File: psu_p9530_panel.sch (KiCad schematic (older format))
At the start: 56 parts, among them IC306 LTC1658, IC308 CD4052B, IC310 TLC272, IC312 TLC272, U401 74HCT164

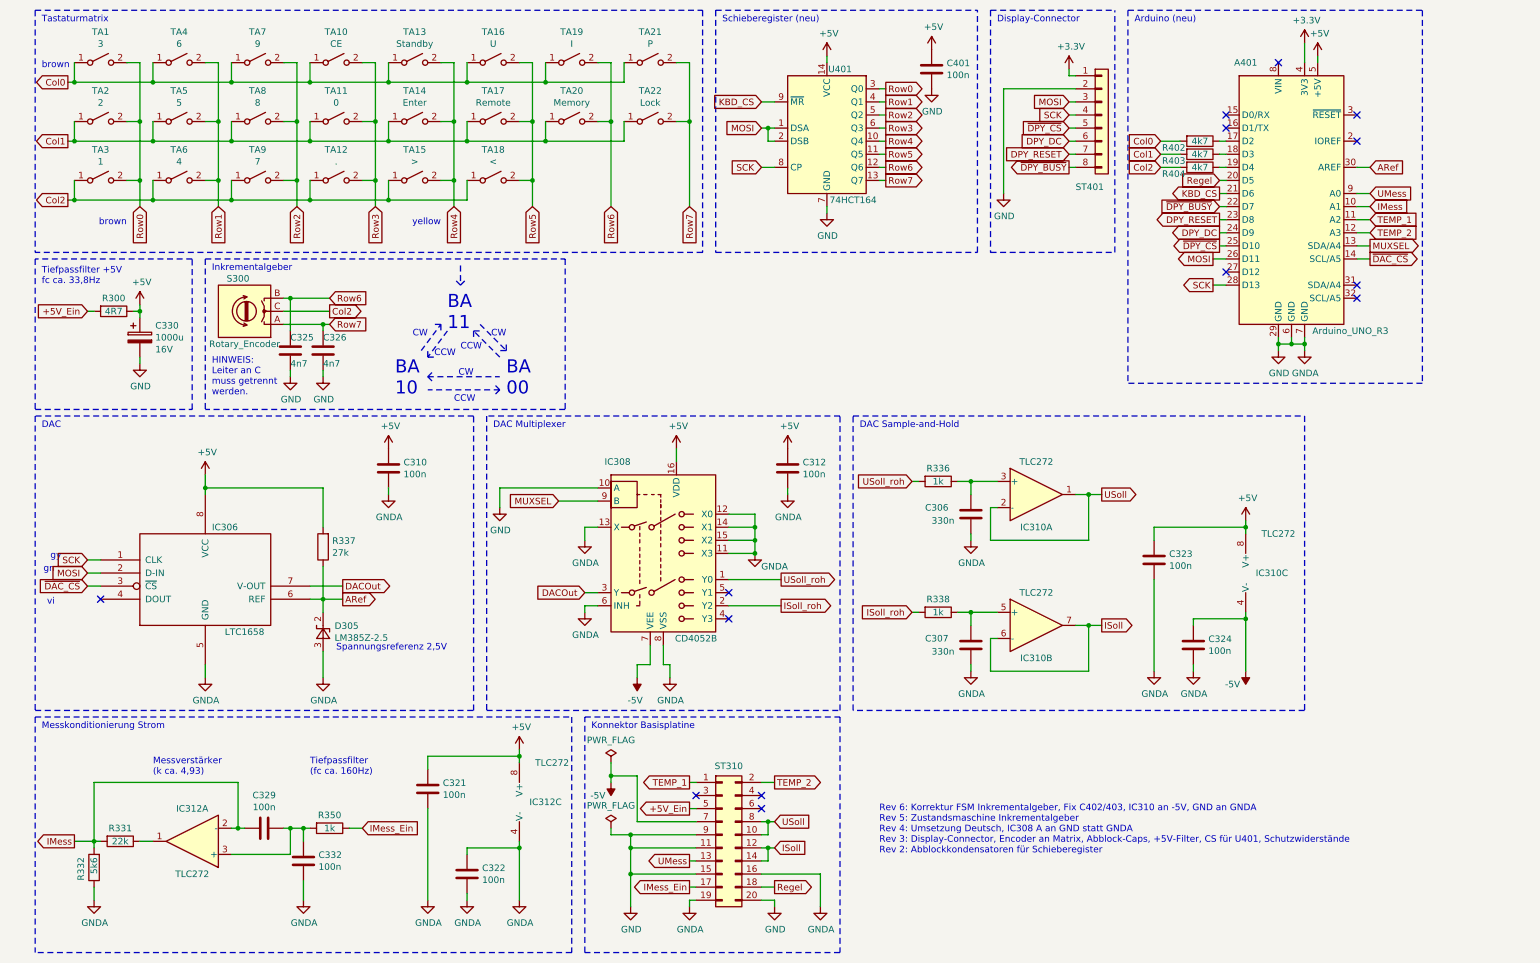
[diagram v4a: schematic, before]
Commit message: Add note about using 54LS164 for the shift register - after half a day of investigations
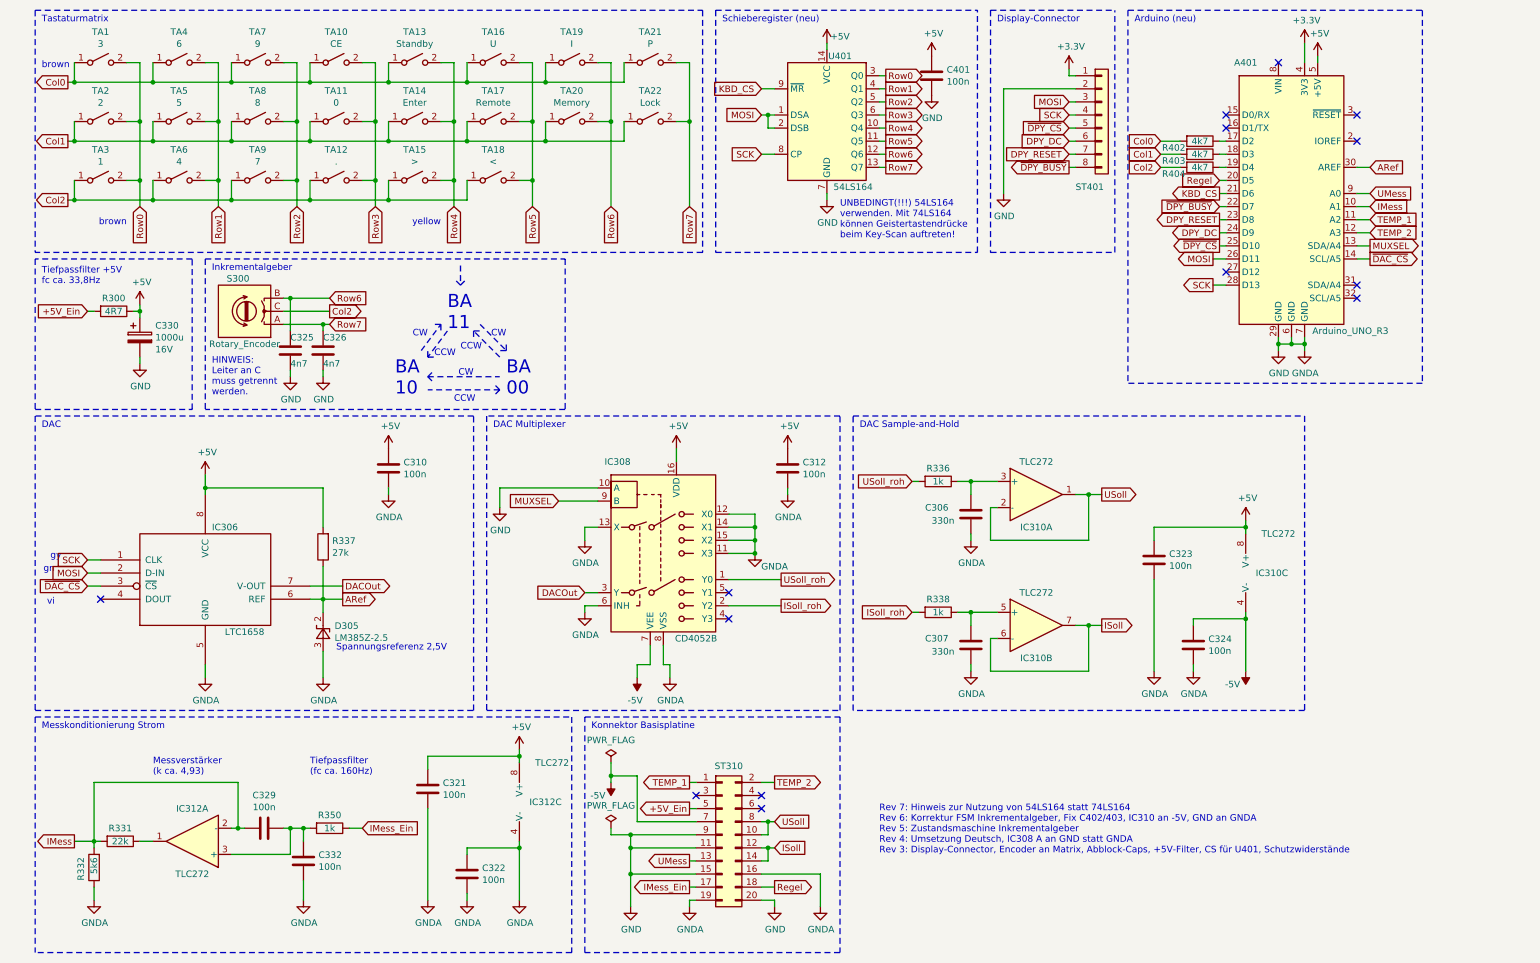
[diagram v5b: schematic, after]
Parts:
- U401: value 74HCT164 -> 54LS164
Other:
- note added: "Rev 7: Hinweis zur Nutzung von 54LS164 statt 74LS164\nRev 6: Korrektur FSM Inkrementalgeber, Fix C402/403, IC310 an -5V, GND an GNDA\nRev 5: Zustandsmaschine Inkrementalgeber\nRev 4: Umsetzung Deutsch, IC308 A an GND statt GNDA\nRev 3: Display-Connector, Encoder an Matrix, Abblock-Caps, +5V-Filter, CS für U401, Schutzwiderstände"
- note added: "UNBEDINGT(!!!) 54LS164\nverwenden. Mit 74LS164\nkönnen Geistertastendrücke\nbeim Key-Scan auftreten!"
- note removed: "Rev 6: Korrektur FSM Inkrementalgeber, Fix C402/403, IC310 an -5V, GND an GNDA\nRev 5: Zustandsmaschine Inkrementalgeber\nRev 4: Umsetzung Deutsch, IC308 A an GND statt GNDA\nRev 3: Display-Connector, Encoder an Matrix, Abblock-Caps, +5V-Filter, CS für U401, Schutzwiderstände\nRev 2: Abblockkondensatoren für Schieberegister"
- moved on the sheet: C401, U401
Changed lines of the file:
@@
 Title "ELV PS9530 Ersatz Bedienteil"
 Date "2022-08-20"
-Rev "6"
+Rev "7"
 Comp "Ralf Gerlich"
 Comment1 ""
@@
 L power:+5V #PWR0126
 U 1 1 6362FD60
-P 6600 900
-F 0 "#PWR0126" H 6600 750 50  0001 C CNN
-F 1 "+5V" H 6615 1073 50  0000 C CNN
-F 2 "" H 6600 900 50  0001 C CNN
-F 3 "" H 6600 900 50  0001 C CNN
-	1    6600 900
-	1    0    0    -1
-$EndComp
-Text GLabel 6100 1750 0    50   Input ~ 0
+P 6600 800
+F 0 "#PWR0126" H 6600 650 50  0001 C CNN
+F 1 "+5V" H 6700 850 50  0000 C CNN
+F 2 "" H 6600 800 50  0001 C CNN
+F 3 "" H 6600 800 50  0001 C CNN
+	1    6600 800
+	1    0    0    -1
+$EndComp
+Text GLabel 6100 1650 0    50   Input ~ 0
 SCK
-Text GLabel 6100 1450 0    50   Input ~ 0
+Text GLabel 6100 1350 0    50   Input ~ 0
 MOSI
+Text GLabel 7050 1050 2    50   Output ~ 0
+Row0
+Wire Wire Line
+	7050 1050 7000 1050
 Text GLabel 7050 1150 2    50   Output ~ 0
-Row0
+Row1
+Text GLabel 7050 1250 2    50   Output ~ 0
+Row2
+Text GLabel 7050 1350 2    50   Output ~ 0
+Row3
+Text GLabel 7050 1450 2    50   Output ~ 0
+Row4
+Text GLabel 7050 1550 2    50   Output ~ 0
+Row5
+Text GLabel 7050 1650 2    50   Output ~ 0
+Row6
+Text GLabel 7050 1750 2    50   Output ~ 0
+Row7
+Wire Wire Line
+	7050 1750 7000 1750
+Wire Wire Line
+	7050 1650 7000 1650
+Wire Wire Line
+	7050 1550 7000 1550
+Wire Wire Line
+	7050 1450 7000 1450
+Wire Wire Line
+	7050 1350 7000 1350
+Wire Wire Line
+	7050 1250 7000 1250
 Wire Wire Line
 	7050 1150 7000 1150
-Text GLabel 7050 1250 2    50   Output ~ 0
-Row1
-Text GLabel 7050 1350 2    50   Output ~ 0
-Row2
-Text GLabel 7050 1450 2    50   Output ~ 0
-Row3
-Text GLabel 7050 1550 2    50   Output ~ 0
-Row4
-Text GLabel 7050 1650 2    50   Output ~ 0
-Row5
-Text GLabel 7050 1750 2    50   Output ~ 0
-Row6
-Text GLabel 7050 1850 2    50   Output ~ 0
-Row7
-Wire Wire Line
-	7050 1850 7000 1850
-Wire Wire Line
-	7050 1750 7000 1750
-Wire Wire Line
-	7050 1650 7000 1650
-Wire Wire Line
-	7050 1550 7000 1550
-Wire Wire Line
-	7050 1450 7000 1450
-Wire Wire Line
-	7050 1350 7000 1350
-Wire Wire Line
-	7050 1250 7000 1250
 Text GLabel 10750 2350 2    50   Output ~ 0
 MUXSEL
@@
 L 74xx:74HCT164 U401
 U 1 1 637BAC19
-P 6600 1450
-F 0 "U401" H 6700 1900 50  0000 C CNN
-F 1 "74HCT164" H 6800 900 50  0000 C CNN
-F 2 "" H 7500 1150 50  0001 C CNN
-F 3 "https://assets.nexperia.com/documents/data-sheet/74HC_HCT164.pdf" H 7500 1150 50  0001 C CNN
-	1    6600 1450
-	1    0    0    -1
-$EndComp
-Wire Wire Line
-	6100 1450 6150 1450
-Wire Wire Line
-	6150 1450 6150 1550
-Wire Wire Line
-	6150 1550 6200 1550
-Connection ~ 6150 1450
+P 6600 1350
+F 0 "U401" H 6700 1800 50  0000 C CNN
+F 1 "54LS164" H 6800 800 50  0000 C CNN
+F 2 "" H 7500 1050 50  0001 C CNN
+F 3 "https://www.ti.com/lit/gpn/sn54ls164" H 7500 1050 50  0001 C CNN
+	1    6600 1350
+	1    0    0    -1
+$EndComp
+Wire Wire Line
+	6100 1350 6150 1350
+Wire Wire Line
+	6150 1350 6150 1450
 Wire Wire Line
 	6150 1450 6200 1450
-Wire Wire Line
-	6600 900  6600 950
+Connection ~ 6150 1350
+Wire Wire Line
+	6150 1350 6200 1350
+Wire Wire Line
+	6600 800  6600 850
 $Comp
 L power:GND #PWR0128
 U 1 1 63836346
-P 6600 2100
-F 0 "#PWR0128" H 6600 1850 50  0001 C CNN
-F 1 "GND" H 6605 1927 50  0000 C CNN
-F 2 "" H 6600 2100 50  0001 C CNN
-F 3 "" H 6600 2100 50  0001 C CNN
-	1    6600 2100
-	1    0    0    -1
-$EndComp
-Wire Wire Line
-	6600 2050 6600 2100
-Wire Wire Line
-	6100 1750 6200 1750
+P 6600 2000
+F 0 "#PWR0128" H 6600 1750 50  0001 C CNN
+F 1 "GND" H 6605 1827 50  0000 C CNN
+F 2 "" H 6600 2000 50  0001 C CNN
+F 3 "" H 6600 2000 50  0001 C CNN
+	1    6600 2000
+	1    0    0    -1
+$EndComp
+Wire Wire Line
+	6600 1950 6600 2000
+Wire Wire Line
+	6100 1650 6200 1650
 NoConn ~ 5600 6550
 NoConn ~ 6100 6550
@@
 L power:+5V #PWR01
 U 1 1 63903112
-P 7400 850
-F 0 "#PWR01" H 7400 700 50  0001 C CNN
-F 1 "+5V" H 7415 1023 50  0000 C CNN
-F 2 "" H 7400 850 50  0001 C CNN
-F 3 "" H 7400 850 50  0001 C CNN
-	1    7400 850
+P 7400 900
+F 0 "#PWR01" H 7400 750 50  0001 C CNN
+F 1 "+5V" H 7415 1073 50  0000 C CNN
+F 2 "" H 7400 900 50  0001 C CNN
+F 3 "" H 7400 900 50  0001 C CNN
+	1    7400 900
 	1    0    0    -1
 $EndComp
@@
 L power:GND #PWR02
 U 1 1 63903430
-P 7400 1150
-F 0 "#PWR02" H 7400 900 50  0001 C CNN
-F 1 "GND" H 7405 977 50  0000 C CNN
-F 2 "" H 7400 1150 50  0001 C CNN
-F 3 "" H 7400 1150 50  0001 C CNN
-	1    7400 1150
+P 7400 1200
+F 0 "#PWR02" H 7400 950 50  0001 C CNN
+F 1 "GND" H 7405 1027 50  0000 C CNN
+F 2 "" H 7400 1200 50  0001 C CNN
+F 3 "" H 7400 1200 50  0001 C CNN
+	1    7400 1200
 	1    0    0    -1
 $EndComp
@@
 L Device:C C401
 U 1 1 6390372F
-P 7400 1000
-F 0 "C401" H 7515 1046 50  0000 L CNN
-F 1 "100n" H 7515 955 50  0000 L CNN
-F 2 "" H 7438 850 50  0001 C CNN
-F 3 "~" H 7400 1000 50  0001 C CNN
-	1    7400 1000
+P 7400 1050
+F 0 "C401" H 7515 1096 50  0000 L CNN
+F 1 "100n" H 7515 1005 50  0000 L CNN
+F 2 "" H 7438 900 50  0001 C CNN
+F 3 "~" H 7400 1050 50  0001 C CNN
+	1    7400 1050
 	1    0    0    -1
 $EndComp
@@
 	1750 3600 1750 2450
 Text Notes 7000 7000 0    50   ~ 0
-Rev 6: Korrektur FSM Inkrementalgeber, Fix C402/403, IC310 an -5V, GND an GNDA\nRev 5: Zustandsmaschine Inkrementalgeber\nRev 4: Umsetzung Deutsch, IC308 A an GND statt GNDA\nRev 3: Display-Connector, Encoder an Matrix, Abblock-Caps, +5V-Filter, CS für U401, Schutzwiderstände\nRev 2: Abblockkondensatoren für Schieberegister
+Rev 7: Hinweis zur Nutzung von 54LS164 statt 74LS164\nRev 6: Korrektur FSM Inkrementalgeber, Fix C402/403, IC310 an -5V, GND an GNDA\nRev 5: Zustandsmaschine Inkrementalgeber\nRev 4: Umsetzung Deutsch, IC308 A an GND statt GNDA\nRev 3: Display-Connector, Encoder an Matrix, Abblock-Caps, +5V-Filter, CS für U401, Schutzwiderstände
 $Comp
 L Device:R R402
@@
 Wire Notes Line
 	8800 2400 8800 550
-Text GLabel 6100 1250 0    50   Input ~ 0
+Text GLabel 6100 1150 0    50   Input ~ 0
 KBD_CS
 Wire Wire Line
-	6100 1250 6200 1250
+	6100 1150 6200 1150
 Text GLabel 9600 1950 0    50   Output ~ 0
 KBD_CS
@@
 Text Notes 700  5100 2    50   ~ 0
 vi
+Text Notes 6700 2300 0    50   ~ 0
+UNBEDINGT(!!!) 54LS164\nverwenden. Mit 74LS164\nkönnen Geistertastendrücke\nbeim Key-Scan auftreten!
 $EndSCHEMATC

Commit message: Fix handling of incremental encoder (again)
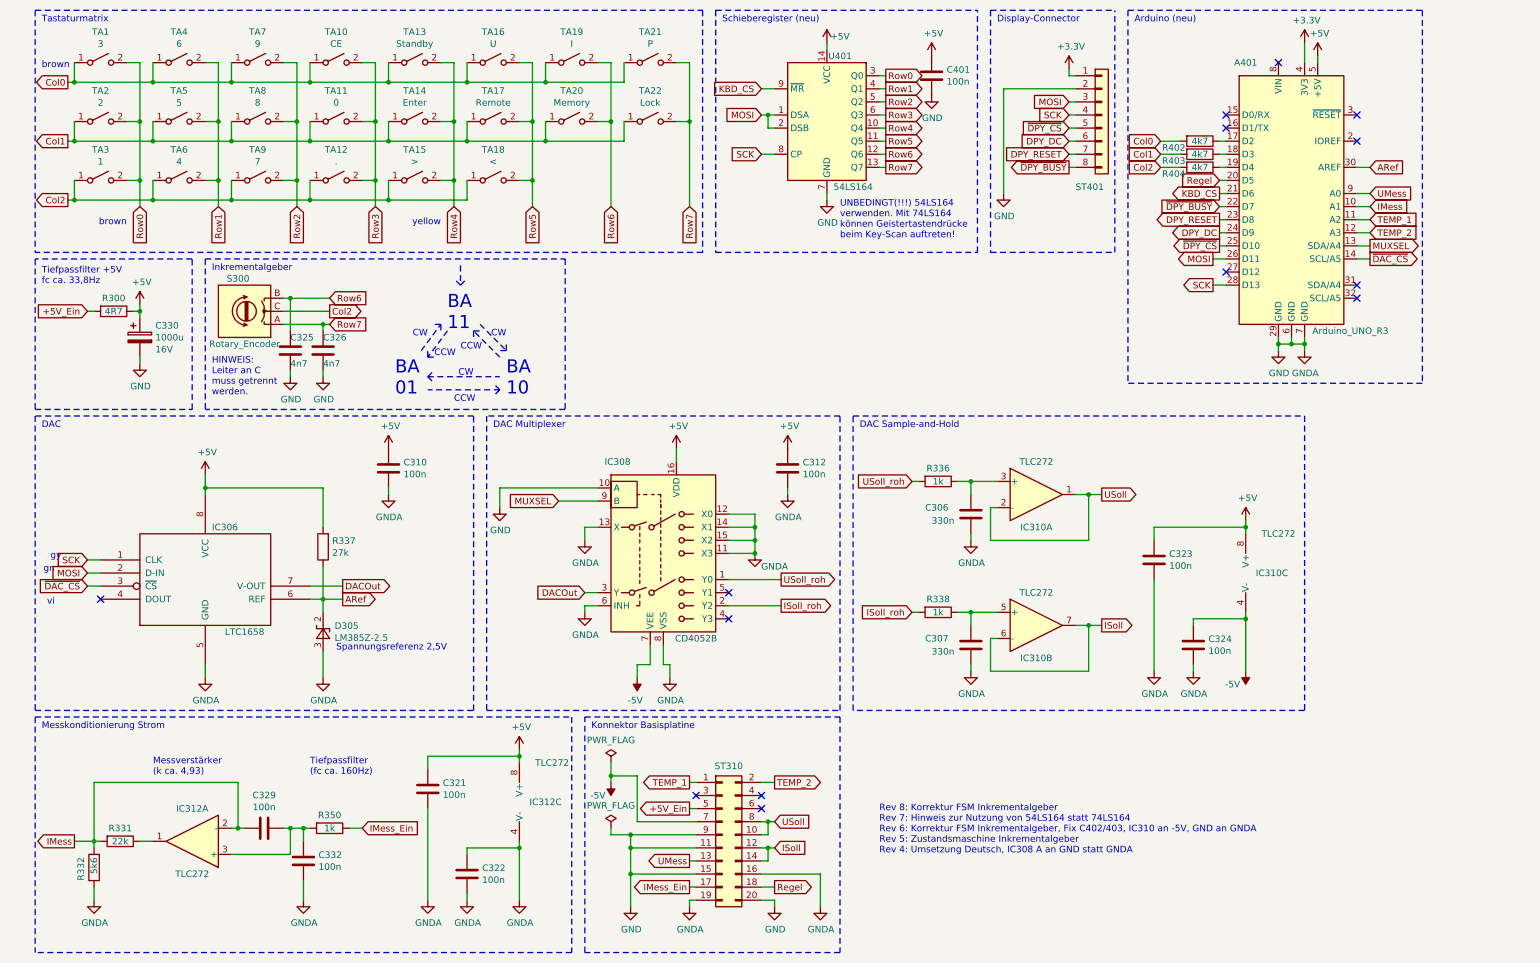
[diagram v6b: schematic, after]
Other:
- note added: "BA\n01"
- note added: "Rev 8: Korrektur FSM Inkrementalgeber\nRev 7: Hinweis zur Nutzung von 54LS164 statt 74LS164\nRev 6: Korrektur FSM Inkrementalgeber, Fix C402/403, IC310 an -5V, GND an GNDA\nRev 5: Zustandsmaschine Inkrementalgeber\nRev 4: Umsetzung Deutsch, IC308 A an GND statt GNDA"
- note removed: "BA\n00"
- note removed: "Rev 7: Hinweis zur Nutzung von 54LS164 statt 74LS164\nRev 6: Korrektur FSM Inkrementalgeber, Fix C402/403, IC310 an -5V, GND an GNDA\nRev 5: Zustandsmaschine Inkrementalgeber\nRev 4: Umsetzung Deutsch, IC308 A an GND statt GNDA\nRev 3: Display-Connector, Encoder an Matrix, Abblock-Caps, +5V-Filter, CS für U401, Schutzwiderstände"
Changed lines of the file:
@@
 Title "ELV PS9530 Ersatz Bedienteil"
 Date "2022-08-20"
-Rev "7"
+Rev "8"
 Comp "Ralf Gerlich"
 Comment1 ""
@@
 	1750 3600 1750 2450
 Text Notes 7000 7000 0    50   ~ 0
-Rev 7: Hinweis zur Nutzung von 54LS164 statt 74LS164\nRev 6: Korrektur FSM Inkrementalgeber, Fix C402/403, IC310 an -5V, GND an GNDA\nRev 5: Zustandsmaschine Inkrementalgeber\nRev 4: Umsetzung Deutsch, IC308 A an GND statt GNDA\nRev 3: Display-Connector, Encoder an Matrix, Abblock-Caps, +5V-Filter, CS für U401, Schutzwiderstände
+Rev 8: Korrektur FSM Inkrementalgeber\nRev 7: Hinweis zur Nutzung von 54LS164 statt 74LS164\nRev 6: Korrektur FSM Inkrementalgeber, Fix C402/403, IC310 an -5V, GND an GNDA\nRev 5: Zustandsmaschine Inkrementalgeber\nRev 4: Umsetzung Deutsch, IC308 A an GND statt GNDA
 $Comp
 L Device:R R402
@@
 brown
 Text Notes 4150 3500 0    100  ~ 0
-BA\n00
+BA\n10
 Text Notes 3300 3500 0    100  ~ 0
-BA\n10
+BA\n01
 Text Notes 3800 3150 0    50   ~ 0
 CCW

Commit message: Encoder to INT0/INT1, change R337, pin updates
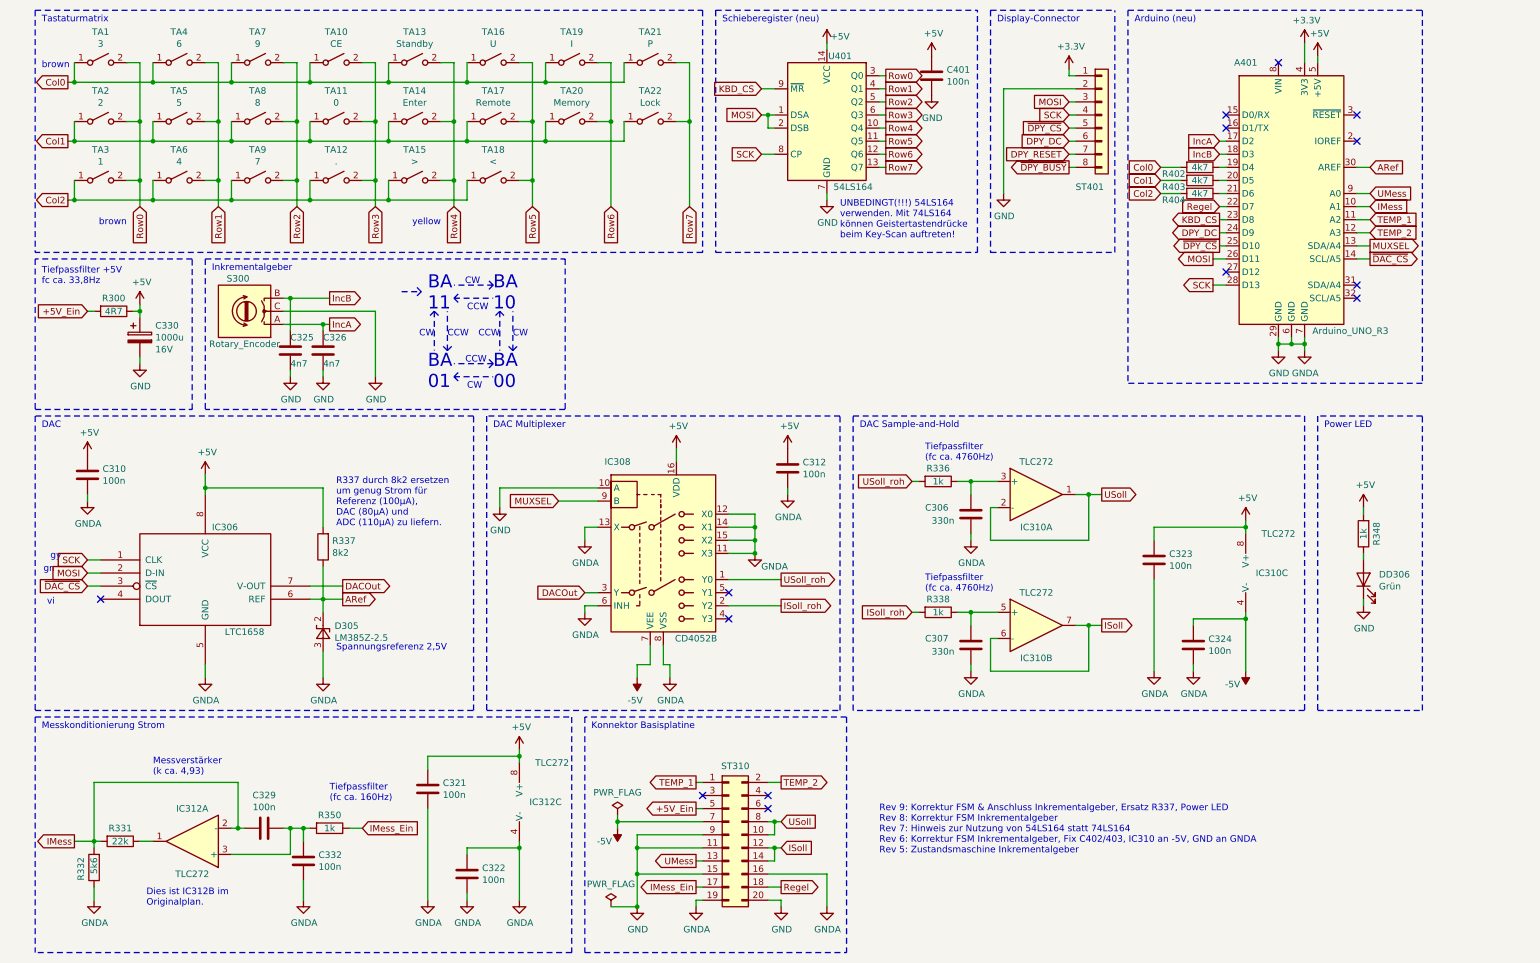
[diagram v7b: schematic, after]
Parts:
- added DD306: Grün, symbol Device:LED
- added R348: 1k, symbol Device:R
- R337: value 27k -> 8k2
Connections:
- net +5V: now also R348.2
- net Col2: no longer S300.C
- net DPY_RESET: no longer A401.23 (D8)
- net GND: now also S300.C, DD306.1 (K)
- net KBD_CS: now also A401.23 (D8); no longer A401.21 (D6)
- net Regel: now also A401.22 (D7); no longer A401.20 (D5)
- net Row6: no longer C325.1, S300.B
- net Row7: no longer C326.1, S300.A
- net ~DPY_BUSY: no longer A401.22 (D7)
- net at R402.1: now also A401.19 (D4); no longer A401.17 (D2)
- net at R403.1: now also A401.20 (D5); no longer A401.18 (D3)
- net at R404.1: now also A401.21 (D6); no longer A401.19 (D4)
- new net: DD306.2 (A), R348.1
- new net IncA: A401.17 (D2), C326.1, S300.A
- new net IncB: A401.18 (D3), C325.1, S300.B
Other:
- note added: "BA\n00"
- note added: "Dies ist IC312B im\nOriginalplan."
- note added: "Power LED"
- note added: "R337 durch 8k2 ersetzen\num genug Strom für\nReferenz (100µA),\nDAC (80µA) und\nADC (110µA) zu liefern."
- note added: "Rev 9: Korrektur FSM & Anschluss Inkrementalgeber, Ersatz R337, Power LED\nRev 8: Korrektur FSM Inkrementalgeber\nRev 7: Hinweis zur Nutzung von 54LS164 statt 74LS164\nRev 6: Korrektur FSM Inkrementalgeber, Fix C402/403, IC310 an -5V, GND an GNDA\nRev 5: Zustandsmaschine Inkrementalgeber"
- note added: "Tiefpassfilter\n(fc ca. 4760Hz)"
- note removed: "HINWEIS:\nLeiter an C\nmuss getrennt\nwerden."
- note removed: "Rev 8: Korrektur FSM Inkrementalgeber\nRev 7: Hinweis zur Nutzung von 54LS164 statt 74LS164\nRev 6: Korrektur FSM Inkrementalgeber, Fix C402/403, IC310 an -5V, GND an GNDA\nRev 5: Zustandsmaschine Inkrementalgeber\nRev 4: Umsetzung Deutsch, IC308 A an GND statt GNDA"
- moved on the sheet: C310, R402, R403, R404, ST310
